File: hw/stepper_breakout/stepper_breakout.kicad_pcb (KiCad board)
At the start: 2 copper layers, 72.4 x 132.1 mm, 56 parts, among them P1 X_HOME, P10 A, P11 Y, P12 POWER_IN, P13 B, P14 X, P15 CONN_02X25, P2 Y_HOME, P3 Z_HOME, P4 A_HOME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

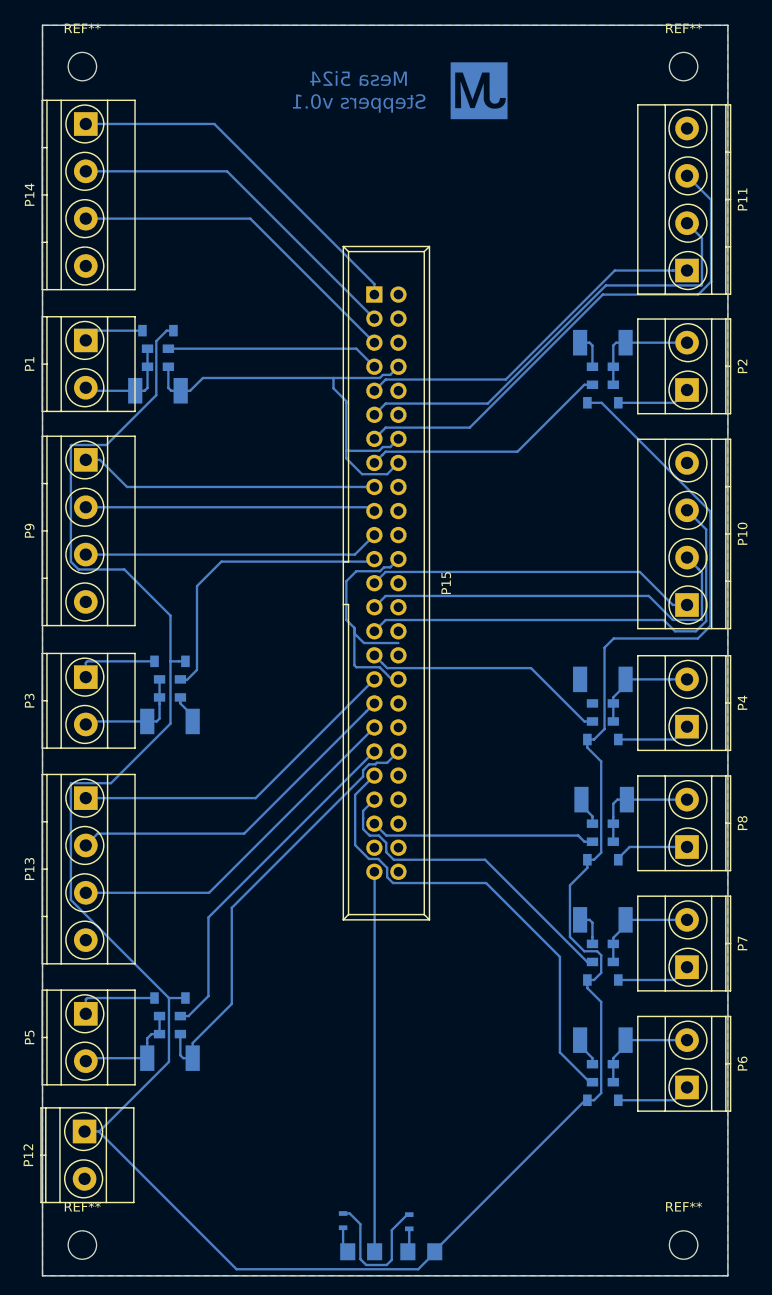
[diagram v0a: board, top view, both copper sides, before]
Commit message: Adjust track width in stepper breakout
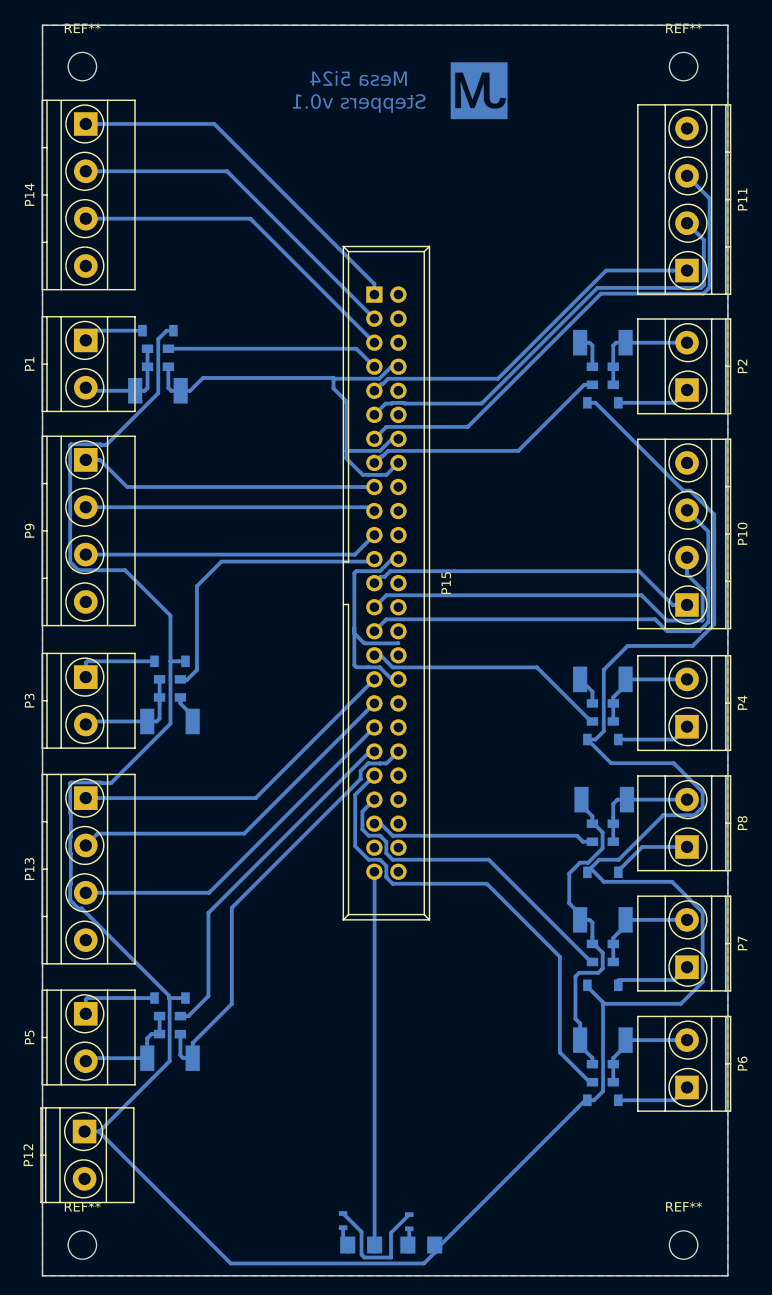
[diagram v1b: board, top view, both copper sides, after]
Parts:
- moved U7 1.32 mm to (118.1, 132.1)
- moved D1 0.71 mm to (98.9, 171.5)
- moved D2 0.71 mm to (92.6, 171.5)
- moved U6 0.56 mm to (118.1, 144.1)
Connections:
- P15 pad 44: (no net) -> GND
- P15 pad 46: (no net) -> GND
- P15 pad 48: (no net) -> GND
- P15 pad 50: (no net) -> GND
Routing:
- net +12V: track 281.1 -> 312.6 mm
- net GND: track 154.2 -> 181.6 mm
- net /E_STOP/SWITCH_A: track 7.90 -> 8.45 mm
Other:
- net class Default: trace_width 0.25 -> 0.4

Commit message: Tweak power and breakout boards a little
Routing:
- net GND: track 181.6 -> 173.5 mm
- net +12V: track 312.6 -> 314.4 mm
